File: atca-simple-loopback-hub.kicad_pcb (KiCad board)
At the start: 12 copper layers, 99.9 x 193 mm, 16 parts, among them J1 0826-1X4T-HS-F, J2 0826-1X4T-HS-F, J20 TE_64690XX-1_J20, J21 TE_64690XX-1_J21, J22 TE_64690XX-1_J22, J23 TE_64690XX-1_J23, J24 TE_64690XX-1_J24, J3 ESD_strip_bottom, K2 Key_K1_K2_TE_1-1469373-1, P10 1766500-1

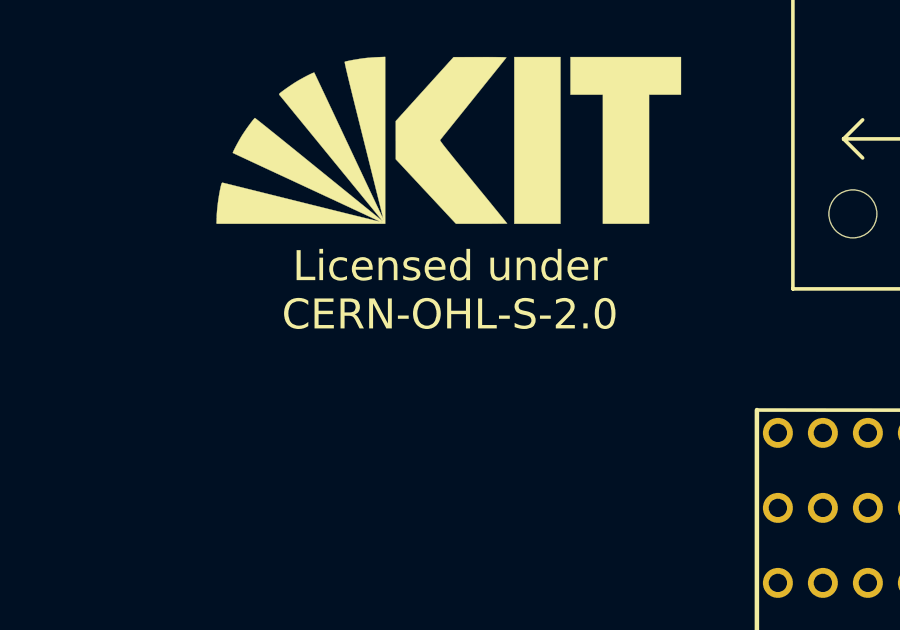
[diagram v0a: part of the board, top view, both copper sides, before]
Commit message: organization of sub sheets
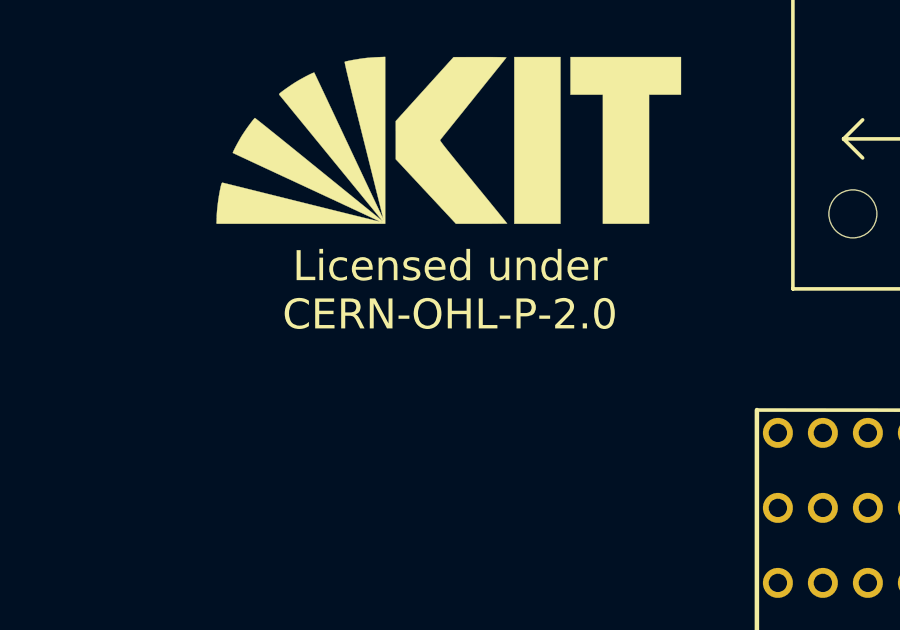
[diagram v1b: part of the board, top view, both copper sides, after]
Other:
- board text added: "Licensed under CERN-OHL-P-2.0"
- board text removed: "Componen keepout 1mm"
- board text removed: "Fabric Channel 1 tuned to 142mm Fabric Channel 2 tuned to 111mm Fabric Channel 3 tuned to 165mm Fabric Channel 4 tuned to 243mm Fabric Channel 5 tuned to 158mm Fabric Channel 6 tuned to 191mm Fabric Channel 10 tuned to 167mm Fabric Channel 15 tuned to 197mm"
- board text removed: "Licensed under CERN-OHL-S-2.0"
- board text removed: "RGMII length matched to 57mm Z3_ETH length matched to 135mm Z3_SATA length matched to 56mm Base Ethernet tuned to 110mm"
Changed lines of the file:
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@@
     (48 "B.Fab" user)
     (49 "F.Fab" user)
-    (50 "User.1" user)
-    (51 "User.2" user)
-    (52 "User.3" user)
-    (53 "User.4" user)
-    (54 "User.5" user)
-    (55 "User.6" user)
-    (56 "User.7" user)
-    (57 "User.8" user)
-    (58 "User.9" user)
   )
   (setup
@@
     )
   )
-  (footprint "project:ESD_strip_bottom" (layer "F.Cu")
+  (footprint "project:ESD_strip_bottom" locked (layer "F.Cu")
     (at 376.499998 350.000005)
     (property "Sheetfile" "sch/mech.kicad_sch")
@@
     (fp_line (start 0 3.556) (end -2.032 5.588)
       (stroke (width 0.1) (type default)) (layer "Dwgs.User"))
-    (pad "1" smd custom (at -5.028 2.992) (size 1 1) (layers "F.Cu" "F.Mask")
+    (pad "1" smd custom locked (at -5.028 2.992) (size 1 1) (layers "F.Cu" "F.Mask")
       (net 207 "/mech/ESD1") (pinfunction "1") (pintype "passive") (zone_connect 0) (thermal_bridge_angle 45)
       (options (clearance outline) (anchor rect))
@@
           (width 0) (fill yes))
       ))
-    (pad "2" smd custom (at -43 3.5) (size 1 1) (layers "F.Cu" "F.Mask")
+    (pad "2" smd custom locked (at -43 3.5) (size 1 1) (layers "F.Cu" "F.Mask")
       (net 208 "/mech/ESD2") (pinfunction "2") (pintype "passive") (zone_connect 0) (thermal_bridge_angle 45)
       (options (clearance outline) (anchor rect))
@@
           (width 0) (fill yes))
       ))
-    (pad "3" smd custom (at -79 3.5) (size 1 1) (layers "F.Cu" "F.Mask")
+    (pad "3" smd custom locked (at -79 3.5) (size 1 1) (layers "F.Cu" "F.Mask")
       (net 65 "GNDPWR") (pinfunction "3") (pintype "passive") (zone_connect 0) (thermal_bridge_angle 45)
       (options (clearance outline) (anchor rect))
@@
   (gr_line (start 276.499998 162.500005) (end 276.499998 355.500005)
     (stroke (width 0.1) (type default)) (layer "Edge.Cuts"))
-  (gr_text "Licensed under \nCERN-OHL-S-2.0" (at 347.499998 175.000005) (layer "F.SilkS")
+  (gr_text "Licensed under \nCERN-OHL-P-2.0" (at 347.499998 175.000005) (layer "F.SilkS")
     (effects (font (size 1 1) (thickness 0.15)))
   )
@@
     (effects (font (size 1.5 1.5) (thickness 0.1)) (justify left top))
   )
-  (gr_text "Componen keepout 1mm" (at 376.86 205.22 90) (layer "Cmts.User")
-    (effects (font (size 1 1) (thickness 0.15)))
-  )
   (gr_text "0" (at 550.128572 252.935) (layer "Cmts.User")
     (effects (font (size 1.5 1.5) (thickness 0.1)) (justify left top))
@@
     (effects (font (size 1.5 1.5) (thickness 0.1)) (justify left top))
   )
-  (gr_text "Componen keepout 1mm" (at 376.86 291.58 90) (layer "Cmts.User")
-    (effects (font (size 1 1) (thickness 0.15)))
-  )
   (gr_text "Verlustwinkel" (at 550.128572 236.375) (layer "Cmts.User")
     (effects (font (size 1.5 1.5) (thickness 0.3)) (justify left top))
@@
     (effects (font (size 1.5 1.5) (thickness 0.1)) (justify left top))
   )
-  (gr_text "Fabric Channel 1 tuned to 142mm\nFabric Channel 2 tuned to 111mm\nFabric Channel 3 tuned to 165mm\nFabric Channel 4 tuned to 243mm\n\nFabric Channel 5 tuned to 158mm\nFabric Channel 6 tuned to 191mm\nFabric Channel 10 tuned to 167mm\nFabric Channel 15 tuned to 197mm" (at 402.75 231.25) (layer "Cmts.User")
-    (effects (font (size 1 1) (thickness 0.15)))
-  )
   (gr_text "PCB thickness 2,4 mm\nSide 1: 21,33 mm max component height\nSide 2: 3,4 mm max component height (cover)" (at 510.478572 216.745) (layer "Cmts.User")
     (effects (font (size 1 1) (thickness 0.15)))
   )
-  (gr_text "RGMII length matched to 57mm\nZ3_ETH length matched to 135mm\nZ3_SATA length matched to 56mm\nBase Ethernet tuned to 110mm" (at 402 219) (layer "Cmts.User")
-    (effects (font (size 1 1) (thickness 0.15)))
-  )

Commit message: sfp+ sheet
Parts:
- added C1: 0.1uF, Capacitor_SMD:C_0402_1005Metric, F.Cu at (256.3, 128.6)
- added C2: 0.1uF, Capacitor_SMD:C_0402_1005Metric, F.Cu at (256.3, 130.5)
- added C3: 0.1uF, Capacitor_SMD:C_0402_1005Metric, F.Cu at (256.3, 132.5)
- added C4: 0.1uF, Capacitor_SMD:C_0402_1005Metric, F.Cu at (256.3, 134.5)
- added C5: 0.1uF, Capacitor_SMD:C_0402_1005Metric, F.Cu at (256.3, 136.4)
- added C6: 0.1uF, Capacitor_SMD:C_0402_1005Metric, F.Cu at (256.3, 138.4)
- added J10: Conn_Coaxial, Connector_Coaxial:MMCX_Molex_73415-1471_Vertical, F.Cu at (315.0, 223.2)
- added J11: Conn_Coaxial, Connector_Coaxial:MMCX_Molex_73415-1471_Vertical, F.Cu at (315.0, 213.5)
- added J12: Conn_Coaxial, Connector_Coaxial:MMCX_Molex_73415-1471_Vertical, F.Cu at (315.0, 203.8)
- added J13: Conn_Coaxial, Connector_Coaxial:MMCX_Molex_73415-1471_Vertical, F.Cu at (315.0, 194.1)
- added J4: Conn_Coaxial, Connector_Coaxial:MMCX_Molex_73415-1471_Vertical, F.Cu at (315.0, 262.0)
- added J5: Conn_Coaxial, Connector_Coaxial:MMCX_Molex_73415-1471_Vertical, F.Cu at (315.0, 252.3)
- added J6: SFP+, project:TE_1888247-1, F.Cu at (246.3, 133.5)
- added J7: SFP+, project:TE_1888247-1, F.Cu at (246.3, 145.6)
- added J8: Conn_Coaxial, Connector_Coaxial:MMCX_Molex_73415-1471_Vertical, F.Cu at (315.0, 242.6)
- added J9: Conn_Coaxial, Connector_Coaxial:MMCX_Molex_73415-1471_Vertical, F.Cu at (315.0, 232.9)
- added R1: 4.7k, Resistor_SMD:R_0402_1005Metric, F.Cu at (314.7, 342.0)
- added R10: 4.7k, Resistor_SMD:R_0402_1005Metric, F.Cu at (314.7, 355.9)
- added R11: 10M 2kV, Resistor_SMD:R_2010_5025Metric, F.Cu at (321.9, 343.1)
- added R12: 10M 2kV, Resistor_SMD:R_2010_5025Metric, F.Cu at (321.9, 347.3)
- added R2: 4.7k, Resistor_SMD:R_0402_1005Metric, F.Cu at (314.7, 344.0)
- added R3: 4.7k, Resistor_SMD:R_0402_1005Metric, F.Cu at (314.7, 346.0)
- added R6: 4.7k, Resistor_SMD:R_0402_1005Metric, F.Cu at (314.7, 348.0)
- added R7: 4.7k, Resistor_SMD:R_0402_1005Metric, F.Cu at (314.7, 349.9)
- added R8: 4.7k, Resistor_SMD:R_0402_1005Metric, F.Cu at (314.7, 351.9)
- added R9: 4.7k, Resistor_SMD:R_0402_1005Metric, F.Cu at (314.7, 353.9)
- added U1: Si5395, Package_DFN_QFN:QFN-64-1EP_9x9mm_P0.5mm_EP5.2x5.2mm, F.Cu at (265.4, 146.5)
- added U2: Si5395, Package_DFN_QFN:QFN-64-1EP_9x9mm_P0.5mm_EP5.2x5.2mm, F.Cu at (265.4, 133.2)
- R4, R5: value 10M 2kV -> 4.7k; footprint Resistor_SMD:R_2010_5025Metric -> Resistor_SMD:R_0402_1005Metric
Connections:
- net /J23/Z2_ETH0.A_N renamed /Z2_BI1.A_N
- net /J23/Z2_ETH0.A_P renamed /Z2_BI1.A_P
- net /J23/Z2_ETH0.B_N renamed /Z2_BI1.B_N
- net /J23/Z2_ETH0.B_P renamed /Z2_BI1.B_P
- net /J23/Z2_ETH0.C_N renamed /Z2_BI1.C_N
- net /J23/Z2_ETH0.C_P renamed /Z2_BI1.C_P
- net /J23/Z2_ETH0.D_N renamed /Z2_BI1.D_N
- net /J23/Z2_ETH0.D_P renamed /Z2_BI1.D_P
- net /J23/Z2_ETH1.A_N renamed /Z2_BI2.A_N
- net /J23/Z2_ETH1.A_P renamed /Z2_BI2.A_P
- net /J23/Z2_ETH1.B_N renamed /Z2_BI2.B_N
- net /J23/Z2_ETH1.B_P renamed /Z2_BI2.B_P
- net /J23/Z2_ETH1.C_N renamed /Z2_BI2.C_N
- net /J23/Z2_ETH1.C_P renamed /Z2_BI2.C_P
- net /J23/Z2_ETH1.D_N renamed /Z2_BI2.D_N
- net /J23/Z2_ETH1.D_P renamed /Z2_BI2.D_P
- J20 pad 10A: unconnected-(J20E-TX0[13]+-Pad10A) -> /Z2_FI13.10GbE_P
- J20 pad 10B: unconnected-(J20E-TX0[13]--Pad10B) -> /Z2_FI13.10GbE_N
- J20 pad 10C: unconnected-(J20E-RX0[13]+-Pad10C) -> /Z2_FI13.10GbE_P
- J20 pad 10D: unconnected-(J20E-RX0[13]--Pad10D) -> /Z2_FI13.10GbE_N
- J20 pad 10E: unconnected-(J20E-TX1[13]+-Pad10E) -> /Z2_FI13.LVDS_P
- J20 pad 10F: unconnected-(J20E-TX1[13]--Pad10F) -> /Z2_FI13.LVDS_N
- J20 pad 10G: unconnected-(J20E-RX1[13]+-Pad10G) -> /Z2_FI13.LVDS_P
- J20 pad 10H: unconnected-(J20E-RX1[13]--Pad10H) -> /Z2_FI13.LVDS_N
- J20 pad 9A: unconnected-(J20E-TX2[13]+-Pad9A) -> /Z2_FI13.TCDS2_P
- J20 pad 9B: unconnected-(J20E-TX2[13]--Pad9B) -> /Z2_FI13.TCDS2_N
- J20 pad 9C: unconnected-(J20E-RX2[13]+-Pad9C) -> /Z2_FI13.TCDS2_P
- J20 pad 9D: unconnected-(J20E-RX2[13]--Pad9D) -> /Z2_FI13.TCDS2_N
- J20 pad 9E: unconnected-(J20E-TX3[13]+-Pad9E) -> /Z2_FI13.LHC_CLK_HQ_P
- J20 pad 9F: unconnected-(J20E-TX3[13]--Pad9F) -> /Z2_FI13.LHC_CLK_HQ_N
- J20 pad 9G: unconnected-(J20E-RX3[13]+-Pad9G) -> /Z2_FI13.LHC_CLK_P
- J20 pad 9H: unconnected-(J20E-RX3[13]--Pad9H) -> /Z2_FI13.LHC_CLK_N
- J21 pad 10A: unconnected-(J21E-TX0[8]+-Pad10A) -> /Z2_FI8.10GbE_P
- J21 pad 10B: unconnected-(J21E-TX0[8]--Pad10B) -> /Z2_FI8.10GbE_N
- J21 pad 10C: unconnected-(J21E-RX0[8]+-Pad10C) -> /Z2_FI8.10GbE_P
- J21 pad 10D: unconnected-(J21E-RX0[8]--Pad10D) -> /Z2_FI8.10GbE_N
- J21 pad 10E: unconnected-(J21E-TX1[8]+-Pad10E) -> /Z2_FI8.LVDS_P
- J21 pad 10F: unconnected-(J21E-TX1[8]--Pad10F) -> /Z2_FI8.LVDS_N
- J21 pad 10G: unconnected-(J21E-RX1[8]+-Pad10G) -> /Z2_FI8.LVDS_P
- J21 pad 10H: unconnected-(J21E-RX1[8]--Pad10H) -> /Z2_FI8.LVDS_N
- J21 pad 1A: unconnected-(J21A-TX2[12]+-Pad1A) -> /Z2_FI12.TCDS2_P
- J21 pad 1B: unconnected-(J21A-TX2[12]--Pad1B) -> /Z2_FI12.TCDS2_N
- J21 pad 1C: unconnected-(J21A-RX2[12]+-Pad1C) -> /Z2_FI12.TCDS2_P
- J21 pad 1D: unconnected-(J21A-RX2[12]--Pad1D) -> /Z2_FI12.TCDS2_N
- J21 pad 1E: unconnected-(J21A-TX3[12]+-Pad1E) -> /Z2_FI12.LHC_CLK_HQ_P
- J21 pad 1F: unconnected-(J21A-TX3[12]--Pad1F) -> /Z2_FI12.LHC_CLK_HQ_N
- J21 pad 1G: unconnected-(J21A-RX3[12]+-Pad1G) -> /Z2_FI12.LHC_CLK_P
- J21 pad 1H: unconnected-(J21A-RX3[12]--Pad1H) -> /Z2_FI12.LHC_CLK_N
- J21 pad 2A: unconnected-(J21A-TX0[12]+-Pad2A) -> /Z2_FI12.10GbE_P
- J21 pad 2B: unconnected-(J21A-TX0[12]--Pad2B) -> /Z2_FI12.10GbE_N
- J21 pad 2C: unconnected-(J21A-RX0[12]+-Pad2C) -> /Z2_FI12.10GbE_P
- J21 pad 2D: unconnected-(J21A-RX0[12]--Pad2D) -> /Z2_FI12.10GbE_N
- J21 pad 2E: unconnected-(J21A-TX1[12]+-Pad2E) -> /Z2_FI12.LVDS_P
- J21 pad 2F: unconnected-(J21A-TX1[12]--Pad2F) -> /Z2_FI12.LVDS_N
- J21 pad 2G: unconnected-(J21A-RX1[12]+-Pad2G) -> /Z2_FI12.LVDS_P
- J21 pad 2H: unconnected-(J21A-RX1[12]--Pad2H) -> /Z2_FI12.LVDS_N
- J21 pad 3A: unconnected-(J21B-TX2[11]+-Pad3A) -> /Z2_FI11.TCDS2_P
- J21 pad 3B: unconnected-(J21B-TX2[11]--Pad3B) -> /Z2_FI11.TCDS2_N
- J21 pad 3C: unconnected-(J21B-RX2[11]+-Pad3C) -> /Z2_FI11.TCDS2_P
- J21 pad 3D: unconnected-(J21B-RX2[11]--Pad3D) -> /Z2_FI11.TCDS2_N
- J21 pad 3E: unconnected-(J21B-TX3[11]+-Pad3E) -> /Z2_FI11.LHC_CLK_HQ_P
- J21 pad 3F: unconnected-(J21B-TX3[11]--Pad3F) -> /Z2_FI11.LHC_CLK_HQ_N
- J21 pad 3G: unconnected-(J21B-RX3[11]+-Pad3G) -> /Z2_FI11.LHC_CLK_P
- J21 pad 3H: unconnected-(J21B-RX3[11]--Pad3H) -> /Z2_FI11.LHC_CLK_N
- J21 pad 4A: unconnected-(J21B-TX0[11]+-Pad4A) -> /Z2_FI11.10GbE_P
- J21 pad 4B: unconnected-(J21B-TX0[11]--Pad4B) -> /Z2_FI11.10GbE_N
- J21 pad 4C: unconnected-(J21B-RX0[11]+-Pad4C) -> /Z2_FI11.10GbE_P
- J21 pad 4D: unconnected-(J21B-RX0[11]--Pad4D) -> /Z2_FI11.10GbE_N
- J21 pad 4E: unconnected-(J21B-TX1[11]+-Pad4E) -> /Z2_FI11.LVDS_P
- J21 pad 4F: unconnected-(J21B-TX1[11]--Pad4F) -> /Z2_FI11.LVDS_N
- J21 pad 4G: unconnected-(J21B-RX1[11]+-Pad4G) -> /Z2_FI11.LVDS_P
- J21 pad 4H: unconnected-(J21B-RX1[11]--Pad4H) -> /Z2_FI11.LVDS_N
- J21 pad 5A: unconnected-(J21C-TX2[10]+-Pad5A) -> /Z2_FI10.TCDS2_P
- J21 pad 5B: unconnected-(J21C-TX2[10]--Pad5B) -> /Z2_FI10.TCDS2_N
- J21 pad 5C: unconnected-(J21C-RX2[10]+-Pad5C) -> /Z2_FI10.TCDS2_P
- J21 pad 5D: unconnected-(J21C-RX2[10]--Pad5D) -> /Z2_FI10.TCDS2_N
- J21 pad 5E: unconnected-(J21C-TX3[10]+-Pad5E) -> /Z2_FI10.LHC_CLK_HQ_P
- J21 pad 5F: unconnected-(J21C-TX3[10]--Pad5F) -> /Z2_FI10.LHC_CLK_HQ_N
- J21 pad 5G: unconnected-(J21C-RX3[10]+-Pad5G) -> /Z2_FI10.LHC_CLK_P
- J21 pad 5H: unconnected-(J21C-RX3[10]--Pad5H) -> /Z2_FI10.LHC_CLK_N
- J21 pad 6A: unconnected-(J21C-TX0[10]+-Pad6A) -> /Z2_FI10.10GbE_P
- J21 pad 6B: unconnected-(J21C-TX0[10]--Pad6B) -> /Z2_FI10.10GbE_N
- J21 pad 6C: unconnected-(J21C-RX0[10]+-Pad6C) -> /Z2_FI10.10GbE_P
- J21 pad 6D: unconnected-(J21C-RX0[10]--Pad6D) -> /Z2_FI10.10GbE_N
- J21 pad 6E: unconnected-(J21C-TX1[10]+-Pad6E) -> /Z2_FI10.LVDS_P
- J21 pad 6F: unconnected-(J21C-TX1[10]--Pad6F) -> /Z2_FI10.LVDS_N
- J21 pad 6G: unconnected-(J21C-RX1[10]+-Pad6G) -> /Z2_FI10.LVDS_P
- J21 pad 6H: unconnected-(J21C-RX1[10]--Pad6H) -> /Z2_FI10.LVDS_N
- J21 pad 7A: unconnected-(J21D-TX2[9]+-Pad7A) -> /Z2_FI9.TCDS2_P
- J21 pad 7B: unconnected-(J21D-TX2[9]--Pad7B) -> /Z2_FI9.TCDS2_N
- J21 pad 7C: unconnected-(J21D-RX2[9]+-Pad7C) -> /Z2_FI9.TCDS2_P
- J21 pad 7D: unconnected-(J21D-RX2[9]--Pad7D) -> /Z2_FI9.TCDS2_N
- J21 pad 7E: unconnected-(J21D-TX3[9]+-Pad7E) -> /Z2_FI9.LHC_CLK_HQ_P
- J21 pad 7F: unconnected-(J21D-TX3[9]--Pad7F) -> /Z2_FI9.LHC_CLK_HQ_N
- J21 pad 7G: unconnected-(J21D-RX3[9]+-Pad7G) -> /Z2_FI9.LHC_CLK_P
- J21 pad 7H: unconnected-(J21D-RX3[9]--Pad7H) -> /Z2_FI9.LHC_CLK_N
- J21 pad 8A: unconnected-(J21D-TX0[9]+-Pad8A) -> /Z2_FI9.10GbE_P
- J21 pad 8B: unconnected-(J21D-TX0[9]--Pad8B) -> /Z2_FI9.10GbE_N
- J21 pad 8C: unconnected-(J21D-RX0[9]+-Pad8C) -> /Z2_FI9.10GbE_P
- J21 pad 8D: unconnected-(J21D-RX0[9]--Pad8D) -> /Z2_FI9.10GbE_N
- J21 pad 8E: unconnected-(J21D-TX1[9]+-Pad8E) -> /Z2_FI9.LVDS_P
- J21 pad 8F: unconnected-(J21D-TX1[9]--Pad8F) -> /Z2_FI9.LVDS_N
- J21 pad 8G: unconnected-(J21D-RX1[9]+-Pad8G) -> /Z2_FI9.LVDS_P
- J21 pad 8H: unconnected-(J21D-RX1[9]--Pad8H) -> /Z2_FI9.LVDS_N
- J21 pad 9A: unconnected-(J21E-TX2[8]+-Pad9A) -> /Z2_FI8.TCDS2_P
- J21 pad 9B: unconnected-(J21E-TX2[8]--Pad9B) -> /Z2_FI8.TCDS2_N
- J21 pad 9C: unconnected-(J21E-RX2[8]+-Pad9C) -> /Z2_FI8.TCDS2_P
- J21 pad 9D: unconnected-(J21E-RX2[8]--Pad9D) -> /Z2_FI8.TCDS2_N
- J21 pad 9E: unconnected-(J21E-TX3[8]+-Pad9E) -> /Z2_FI8.LHC_CLK_HQ_P
- J21 pad 9F: unconnected-(J21E-TX3[8]--Pad9F) -> /Z2_FI8.LHC_CLK_HQ_N
- J21 pad 9G: unconnected-(J21E-RX3[8]+-Pad9G) -> /Z2_FI8.LHC_CLK_P
- J21 pad 9H: unconnected-(J21E-RX3[8]--Pad9H) -> /Z2_FI8.LHC_CLK_N
- J22 pad 10A: unconnected-(J22E-TX0[3]+-Pad10A) -> /Z2_FI3.10GbE_TX_P
- J22 pad 10B: unconnected-(J22E-TX0[3]--Pad10B) -> /Z2_FI3.10GbE_TX_N
- J22 pad 10C: unconnected-(J22E-RX0[3]+-Pad10C) -> /J22/10GbE_RX_P
- J22 pad 10D: unconnected-(J22E-RX0[3]--Pad10D) -> /J22/10GbE_RX_N
- J22 pad 10E: unconnected-(J22E-TX1[3]+-Pad10E) -> /Z2_FI3.LVDS_TX_P
- J22 pad 10F: unconnected-(J22E-TX1[3]--Pad10F) -> /Z2_FI3.LVDS_TX_N
- J22 pad 10G: unconnected-(J22E-RX1[3]+-Pad10G) -> /J22/LVDS_RX_P
- J22 pad 10H: unconnected-(J22E-RX1[3]--Pad10H) -> /J22/LVDS_RX_N
- J22 pad 1A: unconnected-(J22A-TX2[7]+-Pad1A) -> /Z2_FI7.TCDS2_P
- J22 pad 1B: unconnected-(J22A-TX2[7]--Pad1B) -> /Z2_FI7.TCDS2_N
- J22 pad 1C: unconnected-(J22A-RX2[7]+-Pad1C) -> /Z2_FI7.TCDS2_P
- J22 pad 1D: unconnected-(J22A-RX2[7]--Pad1D) -> /Z2_FI7.TCDS2_N
- J22 pad 1E: unconnected-(J22A-TX3[7]+-Pad1E) -> /Z2_FI7.LHC_CLK_HQ_P
- J22 pad 1F: unconnected-(J22A-TX3[7]--Pad1F) -> /Z2_FI7.LHC_CLK_HQ_N
- J22 pad 1G: unconnected-(J22A-RX3[7]+-Pad1G) -> /Z2_FI7.LHC_CLK_P
- J22 pad 1H: unconnected-(J22A-RX3[7]--Pad1H) -> /Z2_FI7.LHC_CLK_N
- J22 pad 2A: unconnected-(J22A-TX0[7]+-Pad2A) -> /Z2_FI7.10GbE_P
- J22 pad 2B: unconnected-(J22A-TX0[7]--Pad2B) -> /Z2_FI7.10GbE_N
- J22 pad 2C: unconnected-(J22A-RX0[7]+-Pad2C) -> /Z2_FI7.10GbE_P
- J22 pad 2D: unconnected-(J22A-RX0[7]--Pad2D) -> /Z2_FI7.10GbE_N
- J22 pad 2E: unconnected-(J22A-TX1[7]+-Pad2E) -> /Z2_FI7.LVDS_P
- J22 pad 2F: unconnected-(J22A-TX1[7]--Pad2F) -> /Z2_FI7.LVDS_N
- J22 pad 2G: unconnected-(J22A-RX1[7]+-Pad2G) -> /Z2_FI7.LVDS_P
- J22 pad 2H: unconnected-(J22A-RX1[7]--Pad2H) -> /Z2_FI7.LVDS_N
- J22 pad 3A: unconnected-(J22B-TX2[6]+-Pad3A) -> /Z2_FI6.TCDS2_P
- J22 pad 3B: unconnected-(J22B-TX2[6]--Pad3B) -> /Z2_FI6.TCDS2_N
- J22 pad 3C: unconnected-(J22B-RX2[6]+-Pad3C) -> /Z2_FI6.TCDS2_P
- J22 pad 3D: unconnected-(J22B-RX2[6]--Pad3D) -> /Z2_FI6.TCDS2_N
- J22 pad 3E: unconnected-(J22B-TX3[6]+-Pad3E) -> /Z2_FI6.LHC_CLK_HQ_P
- J22 pad 3F: unconnected-(J22B-TX3[6]--Pad3F) -> /Z2_FI6.LHC_CLK_HQ_N
- J22 pad 3G: unconnected-(J22B-RX3[6]+-Pad3G) -> /Z2_FI6.LHC_CLK_P
- J22 pad 3H: unconnected-(J22B-RX3[6]--Pad3H) -> /Z2_FI6.LHC_CLK_N
- J22 pad 4A: unconnected-(J22B-TX0[6]+-Pad4A) -> /Z2_FI6.10GbE_P
- J22 pad 4B: unconnected-(J22B-TX0[6]--Pad4B) -> /Z2_FI6.10GbE_N
- J22 pad 4C: unconnected-(J22B-RX0[6]+-Pad4C) -> /Z2_FI6.10GbE_P
- J22 pad 4D: unconnected-(J22B-RX0[6]--Pad4D) -> /Z2_FI6.10GbE_N
- J22 pad 4E: unconnected-(J22B-TX1[6]+-Pad4E) -> /Z2_FI6.LVDS_P
- J22 pad 4F: unconnected-(J22B-TX1[6]--Pad4F) -> /Z2_FI6.LVDS_N
- J22 pad 4G: unconnected-(J22B-RX1[6]+-Pad4G) -> /Z2_FI6.LVDS_P
- J22 pad 4H: unconnected-(J22B-RX1[6]--Pad4H) -> /Z2_FI6.LVDS_N
- J22 pad 5A: unconnected-(J22C-TX2[5]+-Pad5A) -> /Z2_FI5.TCDS2_P
- J22 pad 5B: unconnected-(J22C-TX2[5]--Pad5B) -> /Z2_FI5.TCDS2_N
- J22 pad 5C: unconnected-(J22C-RX2[5]+-Pad5C) -> /Z2_FI5.TCDS2_P
- J22 pad 5D: unconnected-(J22C-RX2[5]--Pad5D) -> /Z2_FI5.TCDS2_N
- J22 pad 5E: unconnected-(J22C-TX3[5]+-Pad5E) -> /Z2_FI5.LHC_CLK_HQ_P
- J22 pad 5F: unconnected-(J22C-TX3[5]--Pad5F) -> /Z2_FI5.LHC_CLK_HQ_N
- J22 pad 5G: unconnected-(J22C-RX3[5]+-Pad5G) -> /Z2_FI5.LHC_CLK_P
- J22 pad 5H: unconnected-(J22C-RX3[5]--Pad5H) -> /Z2_FI5.LHC_CLK_N
- J22 pad 6A: unconnected-(J22C-TX0[5]+-Pad6A) -> /Z2_FI5.10GbE_P
- J22 pad 6B: unconnected-(J22C-TX0[5]--Pad6B) -> /Z2_FI5.10GbE_N
- J22 pad 6C: unconnected-(J22C-RX0[5]+-Pad6C) -> /Z2_FI5.10GbE_P
- J22 pad 6D: unconnected-(J22C-RX0[5]--Pad6D) -> /Z2_FI5.10GbE_N
- J22 pad 6E: unconnected-(J22C-TX1[5]+-Pad6E) -> /Z2_FI5.LVDS_P
- J22 pad 6F: unconnected-(J22C-TX1[5]--Pad6F) -> /Z2_FI5.LVDS_N
- J22 pad 6G: unconnected-(J22C-RX1[5]+-Pad6G) -> /Z2_FI5.LVDS_P
- J22 pad 6H: unconnected-(J22C-RX1[5]--Pad6H) -> /Z2_FI5.LVDS_N
- J22 pad 7A: unconnected-(J22D-TX2[4]+-Pad7A) -> /Z2_FI4.TCDS2_P
- J22 pad 7B: unconnected-(J22D-TX2[4]--Pad7B) -> /Z2_FI4.TCDS2_N
- J22 pad 7C: unconnected-(J22D-RX2[4]+-Pad7C) -> /Z2_FI4.TCDS2_P
- J22 pad 7D: unconnected-(J22D-RX2[4]--Pad7D) -> /Z2_FI4.TCDS2_N
- J22 pad 7E: unconnected-(J22D-TX3[4]+-Pad7E) -> /Z2_FI4.LHC_CLK_HQ_P
- J22 pad 7F: unconnected-(J22D-TX3[4]--Pad7F) -> /Z2_FI4.LHC_CLK_HQ_N
- J22 pad 7G: unconnected-(J22D-RX3[4]+-Pad7G) -> /Z2_FI4.LHC_CLK_P
- J22 pad 7H: unconnected-(J22D-RX3[4]--Pad7H) -> /Z2_FI4.LHC_CLK_N
- J22 pad 8A: unconnected-(J22D-TX0[4]+-Pad8A) -> /Z2_FI4.10GbE_P
- J22 pad 8B: unconnected-(J22D-TX0[4]--Pad8B) -> /Z2_FI4.10GbE_N
- J22 pad 8C: unconnected-(J22D-RX0[4]+-Pad8C) -> /Z2_FI4.10GbE_P
- J22 pad 8D: unconnected-(J22D-RX0[4]--Pad8D) -> /Z2_FI4.10GbE_N
- J22 pad 8E: unconnected-(J22D-TX1[4]+-Pad8E) -> /Z2_FI4.LVDS_P
- J22 pad 8F: unconnected-(J22D-TX1[4]--Pad8F) -> /Z2_FI4.LVDS_N
- J22 pad 8G: unconnected-(J22D-RX1[4]+-Pad8G) -> /Z2_FI4.LVDS_P
- J22 pad 8H: unconnected-(J22D-RX1[4]--Pad8H) -> /Z2_FI4.LVDS_N
- J22 pad 9A: unconnected-(J22E-TX2[3]+-Pad9A) -> /Z2_FI3.TCDS2_TX_P
- J22 pad 9B: unconnected-(J22E-TX2[3]--Pad9B) -> /Z2_FI3.TCDS2_TX_N
- J22 pad 9C: unconnected-(J22E-RX2[3]+-Pad9C) -> /J22/TCDS2_RX_P
- J22 pad 9D: unconnected-(J22E-RX2[3]--Pad9D) -> /J22/TCDS2_RX_N
- J22 pad 9E: unconnected-(J22E-TX3[3]+-Pad9E) -> /Z2_FI3.LHC_CLK_HQ_P
- J22 pad 9F: unconnected-(J22E-TX3[3]--Pad9F) -> /Z2_FI3.LHC_CLK_HQ_N
- J22 pad 9G: unconnected-(J22E-RX3[3]+-Pad9G) -> /Z2_FI3.LHC_CLK_P
- J22 pad 9H: unconnected-(J22E-RX3[3]--Pad9H) -> /Z2_FI3.LHC_CLK_N
- J23 pad 10A: unconnected-(J23E-Tx0[2]+-Pad10A) -> /Z2_BI6.A_P
- J23 pad 10B: unconnected-(J23E-Tx0[2]--Pad10B) -> /Z2_BI6.A_N
- J23 pad 10C: unconnected-(J23E-Rx0[2]+-Pad10C) -> /Z2_BI6.B_P
- J23 pad 10D: unconnected-(J23E-Rx0[2]--Pad10D) -> /Z2_BI6.B_N
- J23 pad 10E: unconnected-(J23E-Tx1[2]+-Pad10E) -> /Z2_BI6.C_P
- J23 pad 10F: unconnected-(J23E-Tx1[2]--Pad10F) -> /Z2_BI6.C_N
- J23 pad 10G: unconnected-(J23E-Rx1[2]+-Pad10G) -> /Z2_BI6.D_P
- J23 pad 10H: unconnected-(J23E-Rx1[2]--Pad10H) -> /Z2_BI6.D_N
- J23 pad 1A: unconnected-(J23A-Tx2[2]+-Pad1A) -> /Z2_FI2.TCDS2_P
- J23 pad 1B: unconnected-(J23A-Tx2[2]--Pad1B) -> /Z2_FI2.TCDS2_N
- J23 pad 1C: unconnected-(J23A-Rx2[2]+-Pad1C) -> /Z2_FI2.TCDS2_P
- J23 pad 1D: unconnected-(J23A-Rx2[2]--Pad1D) -> /Z2_FI2.TCDS2_N
- J23 pad 1E: unconnected-(J23A-Tx3[2]+-Pad1E) -> /Z2_FI2.LHC_CLK_HQ_P
- J23 pad 1F: unconnected-(J23A-Tx3[2]--Pad1F) -> /Z2_FI2.LHC_CLK_HQ_N
- J23 pad 1G: unconnected-(J23A-Rx3[2]+-Pad1G) -> /Z2_FI2.LHC_CLK_P
- J23 pad 1H: unconnected-(J23A-Rx3[2]--Pad1H) -> /Z2_FI2.LHC_CLK_N
- J23 pad 2A: unconnected-(J23A-Tx0[2]+-Pad2A) -> /Z2_FI2.10GbE_P
- J23 pad 2B: unconnected-(J23A-Tx0[2]--Pad2B) -> /Z2_FI2.10GbE_N
- J23 pad 2C: unconnected-(J23A-Rx0[2]+-Pad2C) -> /Z2_FI2.10GbE_P
- J23 pad 2D: unconnected-(J23A-Rx0[2]--Pad2D) -> /Z2_FI2.10GbE_N
- J23 pad 2E: unconnected-(J23A-Tx1[2]+-Pad2E) -> /Z2_FI2.LVDS_P
- J23 pad 2F: unconnected-(J23A-Tx1[2]--Pad2F) -> /Z2_FI2.LVDS_N
- J23 pad 2G: unconnected-(J23A-Rx1[2]+-Pad2G) -> /Z2_FI2.LVDS_P
- J23 pad 2H: unconnected-(J23A-Rx1[2]--Pad2H) -> /Z2_FI2.LVDS_N
- J23 pad 3A: unconnected-(J23B-Tx2[1]+-Pad3A) -> /Z2_FI1.TCDS2_P
- J23 pad 3B: unconnected-(J23B-Tx2[1]--Pad3B) -> /Z2_FI1.TCDS2_N
- J23 pad 3C: unconnected-(J23B-Rx2[1]+-Pad3C) -> /Z2_FI1.TCDS2_P
- J23 pad 3D: unconnected-(J23B-Rx2[1]--Pad3D) -> /Z2_FI1.TCDS2_N
- J23 pad 3E: unconnected-(J23B-Tx3[1]+-Pad3E) -> /Z2_FI1.LHC_CLK_HQ_P
- J23 pad 3F: unconnected-(J23B-Tx3[1]--Pad3F) -> /Z2_FI1.LHC_CLK_HQ_N
- J23 pad 3G: unconnected-(J23B-Rx3[1]+-Pad3G) -> /Z2_FI1.LHC_CLK_P
- J23 pad 3H: unconnected-(J23B-Rx3[1]--Pad3H) -> /Z2_FI1.LHC_CLK_N
- J23 pad 4A: unconnected-(J23B-Tx0[1]+-Pad4A) -> /Z2_FI1.10GbE_P
- J23 pad 4B: unconnected-(J23B-Tx0[1]--Pad4B) -> /Z2_FI1.10GbE_N
- J23 pad 4C: unconnected-(J23B-Rx0[1]+-Pad4C) -> /Z2_FI1.10GbE_P
- J23 pad 4D: unconnected-(J23B-Rx0[1]--Pad4D) -> /Z2_FI1.10GbE_N
- J23 pad 4E: unconnected-(J23B-Tx1[1]+-Pad4E) -> /Z2_FI1.LVDS_P
- J23 pad 4F: unconnected-(J23B-Tx1[1]--Pad4F) -> /Z2_FI1.LVDS_N
- J23 pad 4G: unconnected-(J23B-Rx1[1]+-Pad4G) -> /Z2_FI1.LVDS_P
- J23 pad 4H: unconnected-(J23B-Rx1[1]--Pad4H) -> /Z2_FI1.LVDS_N
- J23 pad 7A: unconnected-(J23D-Tx2[2]+-Pad7A) -> /Z2_BI3.A_P
- J23 pad 7B: unconnected-(J23D-Tx2[2]--Pad7B) -> /Z2_BI3.A_N
- J23 pad 7C: unconnected-(J23D-Rx2[2]+-Pad7C) -> /Z2_BI3.B_P
- J23 pad 7D: unconnected-(J23D-Rx2[2]--Pad7D) -> /Z2_BI3.B_N
- J23 pad 7E: unconnected-(J23D-Tx3[2]+-Pad7E) -> /Z2_BI3.C_P
- J23 pad 7F: unconnected-(J23D-Tx3[2]--Pad7F) -> /Z2_BI3.C_N
- J23 pad 7G: unconnected-(J23D-Rx3[2]+-Pad7G) -> /Z2_BI3.D_P
- J23 pad 7H: unconnected-(J23D-Rx3[2]--Pad7H) -> /Z2_BI3.D_N
- J23 pad 8A: unconnected-(J23D-Tx0[2]+-Pad8A) -> /Z2_BI4.A_P
- J23 pad 8B: unconnected-(J23D-Tx0[2]--Pad8B) -> /Z2_BI4.A_N
- J23 pad 8C: unconnected-(J23D-Rx0[2]+-Pad8C) -> /Z2_BI4.B_P
- J23 pad 8D: unconnected-(J23D-Rx0[2]--Pad8D) -> /Z2_BI4.B_N
- J23 pad 8E: unconnected-(J23D-Tx1[2]+-Pad8E) -> /Z2_BI4.C_P
- J23 pad 8F: unconnected-(J23D-Tx1[2]--Pad8F) -> /Z2_BI4.C_N
- J23 pad 8G: unconnected-(J23D-Rx1[2]+-Pad8G) -> /Z2_BI4.D_P
- J23 pad 8H: unconnected-(J23D-Rx1[2]--Pad8H) -> /Z2_BI4.D_N
- J23 pad 9A: unconnected-(J23E-Tx2[2]+-Pad9A) -> /Z2_BI5.A_P
- J23 pad 9B: unconnected-(J23E-Tx2[2]--Pad9B) -> /Z2_BI5.A_N
- J23 pad 9C: unconnected-(J23E-Rx2[2]+-Pad9C) -> /Z2_BI5.B_P
- J23 pad 9D: unconnected-(J23E-Rx2[2]--Pad9D) -> /Z2_BI5.B_N
- J23 pad 9E: unconnected-(J23E-Tx3[2]+-Pad9E) -> /Z2_BI5.C_P
- J23 pad 9F: unconnected-(J23E-Tx3[2]--Pad9F) -> /Z2_BI5.C_N
- J23 pad 9G: unconnected-(J23E-Rx3[2]+-Pad9G) -> /Z2_BI5.D_P
- J23 pad 9H: unconnected-(J23E-Rx3[2]--Pad9H) -> /Z2_BI5.D_N
- J24 pad 1A: unconnected-(J24A-BI_DA7+-Pad1A) -> /Z2_BI7.A_P
- J24 pad 1B: unconnected-(J24A-BI_DA7--Pad1B) -> /Z2_BI7.A_N
- J24 pad 1C: unconnected-(J24A-BI_DB7+-Pad1C) -> /Z2_BI7.B_P
- J24 pad 1D: unconnected-(J24A-BI_DB7--Pad1D) -> /Z2_BI7.B_N
- J24 pad 1E: unconnected-(J24A-BI_DC7+-Pad1E) -> /Z2_BI7.C_P
- J24 pad 1F: unconnected-(J24A-BI_DC7--Pad1F) -> /Z2_BI7.C_N
- J24 pad 1G: unconnected-(J24A-BI_DD7+-Pad1G) -> /Z2_BI7.D_P
- J24 pad 1H: unconnected-(J24A-BI_DD7--Pad1H) -> /Z2_BI7.D_N
- J24 pad 2A: unconnected-(J24A-BI_DA8+-Pad2A) -> /Z2_BI8.A_P
- J24 pad 2B: unconnected-(J24A-BI_DA8--Pad2B) -> /Z2_BI8.A_N
- J24 pad 2C: unconnected-(J24A-BI_DB8+-Pad2C) -> /Z2_BI8.B_P
- J24 pad 2D: unconnected-(J24A-BI_DB8--Pad2D) -> /Z2_BI8.B_N
- J24 pad 2E: unconnected-(J24A-BI_DC8+-Pad2E) -> /Z2_BI8.C_P
- J24 pad 2F: unconnected-(J24A-BI_DC8--Pad2F) -> /Z2_BI8.C_N
- J24 pad 2G: unconnected-(J24A-BI_DD8+-Pad2G) -> /Z2_BI8.D_P
- J24 pad 2H: unconnected-(J24A-BI_DD8--Pad2H) -> /Z2_BI8.D_N
- R4 pad 1: /mech/ESD1 -> +3V3
- R4 pad 2: GNDPWR -> /SFP+/SC_SFP+_1.RX_LOS
- R5 pad 1: /mech/ESD2 -> +3V3
- R5 pad 2: GND -> /SFP+/SC_SFP+_1.TX_FAULT

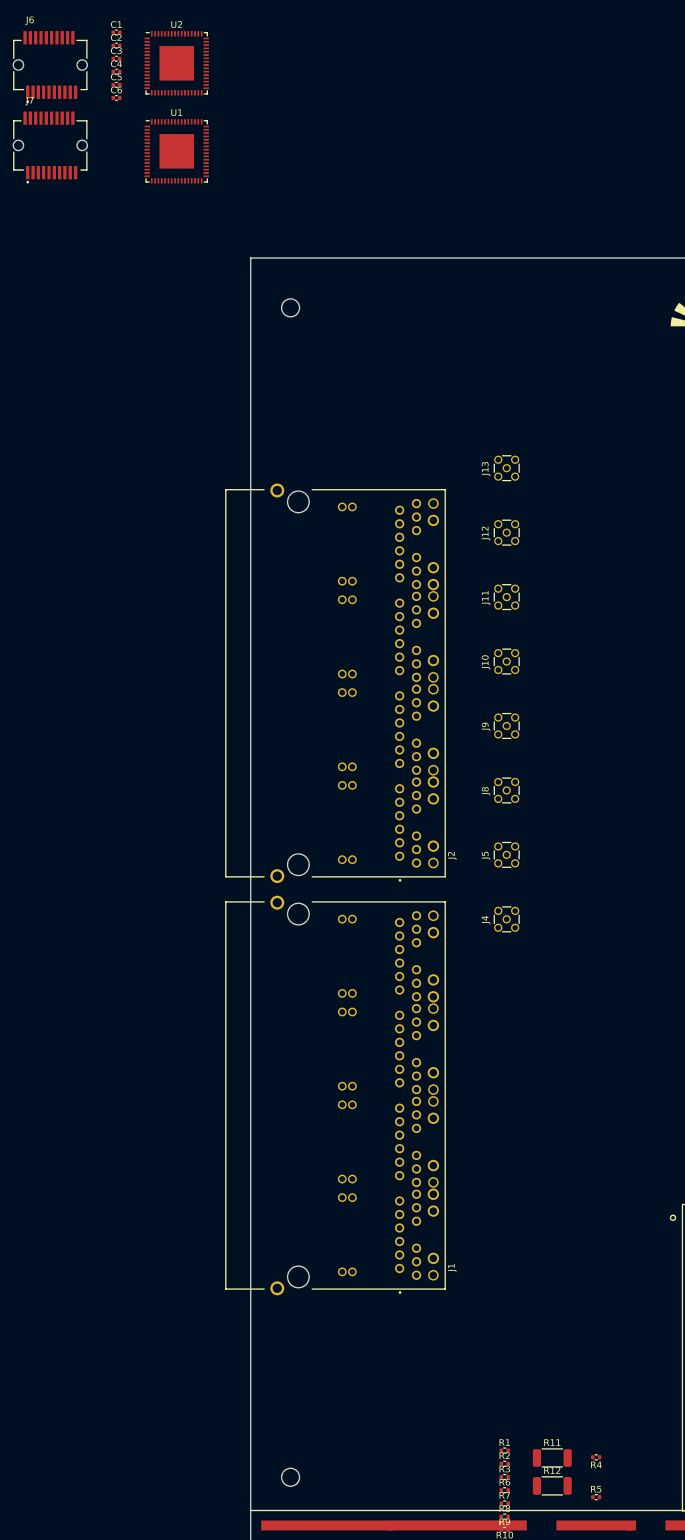
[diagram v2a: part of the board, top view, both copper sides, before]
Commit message: work on sc pll and pll sheet
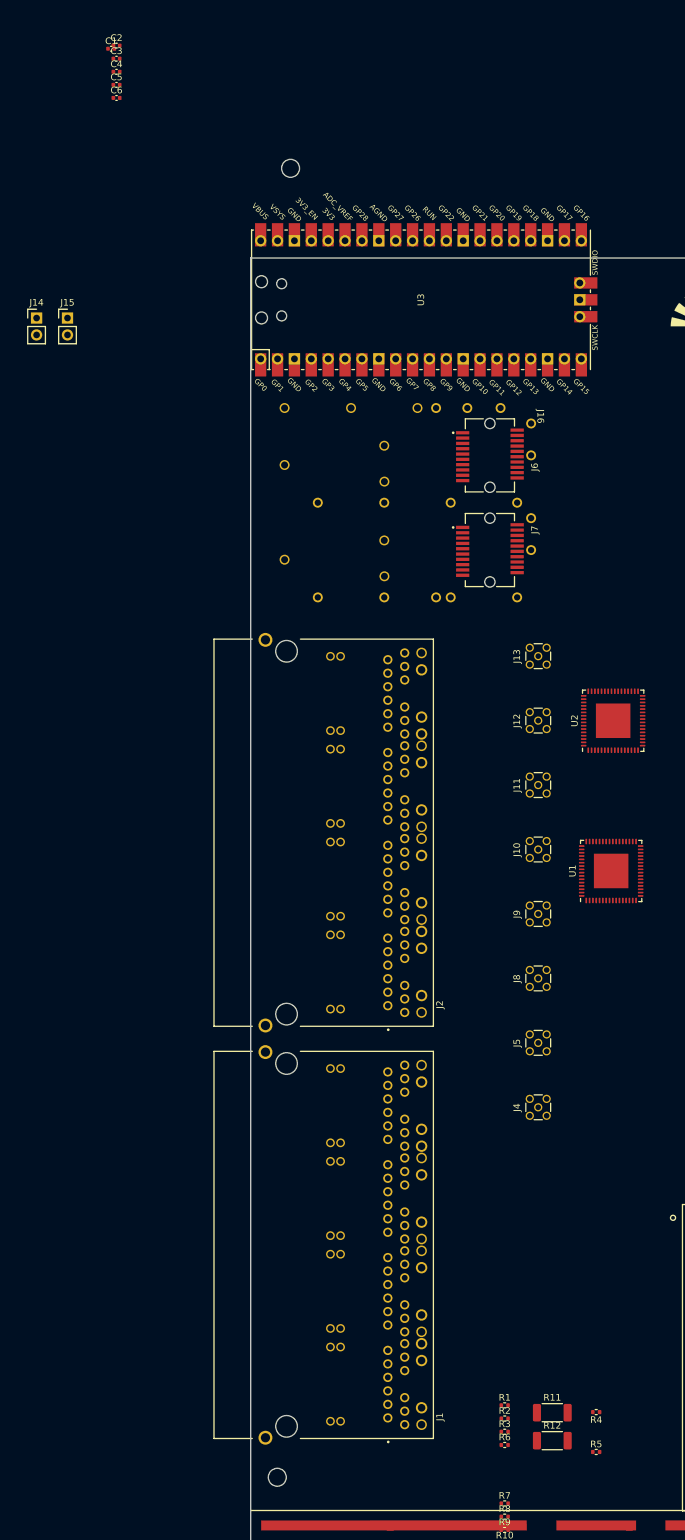
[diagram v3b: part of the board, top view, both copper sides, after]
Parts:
- added J14: Conn_01x02_Pin, Connector_PinHeader_2.54mm:PinHeader_1x02_P2.54mm_Vertical, F.Cu at (244.3, 171.5)
- added J15: Conn_01x02_Pin, Connector_PinHeader_2.54mm:PinHeader_1x02_P2.54mm_Vertical, F.Cu at (248.9, 171.5)
- added J16: TE 2007262-1, project:TE_2007263-1, F.Cu at (312.5, 197.0)
- added U3: Pico, project:RPi_Pico_SMD_TH, F.Cu at (302.1, 168.8)
- moved U1 126.5 mm to (330.7, 254.8), turned to 90 degrees
- moved U2 118.8 mm to (331.0, 232.1), turned to 90 degrees
- moved J7 93.2 mm to (312.5, 211.3), turned to -90 degrees
- moved J6 91.7 mm to (312.5, 197.0), turned to -90 degrees
- moved J11 28.7 mm to (319.8, 241.8)
- moved J9 28.7 mm to (319.8, 261.2)
- moved J10 28.7 mm to (319.8, 251.5)
- moved J12 28.7 mm to (319.8, 232.1)
- moved J13 28.7 mm to (319.8, 222.4)
- moved J5 28.7 mm to (319.8, 280.6)
- moved J8 28.7 mm to (319.8, 270.9)
- moved J4 28.7 mm to (319.8, 290.3)
- moved J1 22.6 mm to (281.9, 311.0)
- moved J2 22.6 mm to (281.9, 249.0)
- moved H3 21.0 mm to (282.5, 149.0)
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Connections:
- J4 pad 1: unconnected-(J4-In-Pad1) -> /LHC_CLK/CLK_IN_P
- J5 pad 1: unconnected-(J5-In-Pad1) -> /LHC_CLK/CLK_IN_N
- J8 pad 1: unconnected-(J8-In-Pad1) -> /LHC_CLK_HQ/CLK_IN_P
- J9 pad 1: unconnected-(J9-In-Pad1) -> /LHC_CLK_HQ/CLK_IN_N
- U1 pad 63: unconnected-(U1-IN0-Pad63) -> /LHC_CLK_HQ/CLK_IN_P
- U1 pad 64: unconnected-(U1-IN0b-Pad64) -> /LHC_CLK_HQ/CLK_IN_N
- U2 pad 63: unconnected-(U2-IN0-Pad63) -> /LHC_CLK/CLK_IN_P
- U2 pad 64: unconnected-(U2-IN0b-Pad64) -> /LHC_CLK/CLK_IN_N
